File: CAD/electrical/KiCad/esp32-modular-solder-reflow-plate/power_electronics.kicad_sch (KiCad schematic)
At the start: 20 parts, among them Q1 Heater N-FET, Q2 Q_PMOS_DGS, U4 AMS1117-3.3, U5 AMS1117-5.0

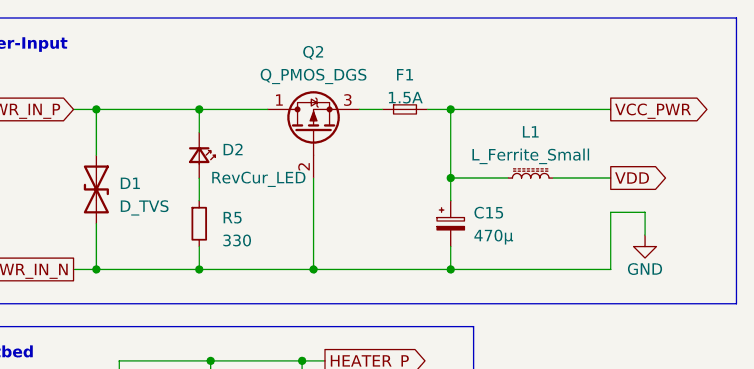
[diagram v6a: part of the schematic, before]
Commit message: - CAD: added usb pd trigger configurable via esp, routing adjustments
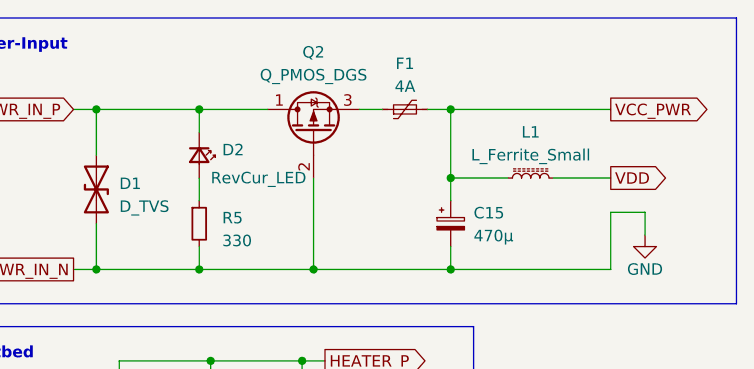
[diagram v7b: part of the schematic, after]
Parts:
- removed F1: 1.5A, Fuse:Fuseholder_Cylinder-5x20mm_Schurter_0031_8201_Horizontal_Open, symbol Device:Fuse_Small
- added F1: 4A, Fuse:Fuse_BelFuse_0ZRE0005FF_L8.3mm_W3.8mm, symbol Device:Polyfuse_Small
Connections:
- net HEATER_P: now also F1.2
- net at Q2.3 (S): now also F1.1
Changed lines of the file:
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@@
-	)
-	(symbol
-		(lib_id "Device:Fuse_Small")
-		(at 67.31 25.4 0)
-		(unit 1)
-		(exclude_from_sim no)
-		(in_bom yes)
-		(on_board yes)
-		(dnp no)
-		(fields_autoplaced yes)
-		(property "Reference" "F1"
-			(at 67.31 21.59 0)
-			(effects
-				(font
-					(size 1.27 1.27)
-				)
-			)
-		)
-		(property "Value" "1.5A"
-			(at 67.31 24.13 0)
-			(effects
-				(font
-					(size 1.27 1.27)
-				)
-			)
-		)
-		(property "Footprint" "Fuse:Fuseholder_Cylinder-5x20mm_Schurter_0031_8201_Horizontal_Open"
-			(at 67.31 25.4 0)
-			(effects
-				(font
-					(size 1.27 1.27)
-				)
-				(hide yes)
-			)
-		)
-		(property "Datasheet" "~"
-			(at 67.31 25.4 0)
-			(effects
-				(font
-					(size 1.27 1.27)
-				)
-				(hide yes)
-			)
-		)
-		(property "Description" ""
-			(at 67.31 25.4 0)
-			(effects
-				(font
-					(size 1.27 1.27)
-				)
-				(hide yes)
-			)
-		)
-		(pin "1"
-		)
-		(pin "2"
-		)
-		(instances
-			(project "esp32-modular-solder-reflow-plate"
-				(path "/33f3a99a-8df0-41a5-be2d-1e3400ca68bb/e7c4b288-cae6-41f4-8e83-3e14eed6f49f"
-					(reference "F1")
-					(unit 1)
-				)
-			)
-			(project "Sperminator_Mk2"
-				(path "/93ce3170-4d90-4483-94fb-ae468b6fbed7"
-					(reference "F?")
-					(unit 1)
-				)
-			)
-		)
 	)
 	(symbol
@@
 					(unit 1)
 				)
+			)
+		)
+	)
+	(symbol
+		(lib_id "Device:Polyfuse_Small")
+		(at 67.31 25.4 90)
+		(unit 1)
+		(exclude_from_sim no)
+		(in_bom yes)
+		(on_board yes)
+		(dnp no)
+		(property "Reference" "F1"
+			(at 67.31 20.32 90)
+			(effects
+				(font
+					(size 1.27 1.27)
+				)
+			)
+		)
+		(property "Value" "4A"
+			(at 67.31 22.86 90)
+			(effects
+				(font
+					(size 1.27 1.27)
+				)
+			)
+		)
+		(property "Footprint" "Fuse:Fuse_BelFuse_0ZRE0005FF_L8.3mm_W3.8mm"
+			(at 72.39 24.13 0)
+			(effects
+				(font
+					(size 1.27 1.27)
+				)
+				(justify left)
+				(hide yes)
+			)
+		)
+		(property "Datasheet" "~"
+			(at 67.31 25.4 0)
+			(effects
+				(font
+					(size 1.27 1.27)
+				)
+				(hide yes)
+			)
+		)
+		(property "Description" "Resettable fuse, polymeric positive temperature coefficient, small symbol"
+			(at 67.31 25.4 0)
+			(effects
+				(font
+					(size 1.27 1.27)
+				)
+				(hide yes)
+			)
+		)
+		(pin "2"
+		)
+		(pin "1"
+		)
+		(instances
+			(project "esp32-modular-solder-reflow-plate"
+				(path "/33f3a99a-8df0-41a5-be2d-1e3400ca68bb/e7c4b288-cae6-41f4-8e83-3e14eed6f49f"
+					(reference "F1")
+					(unit 1)
+				)
